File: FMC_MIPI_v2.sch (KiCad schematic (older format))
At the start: 1 part

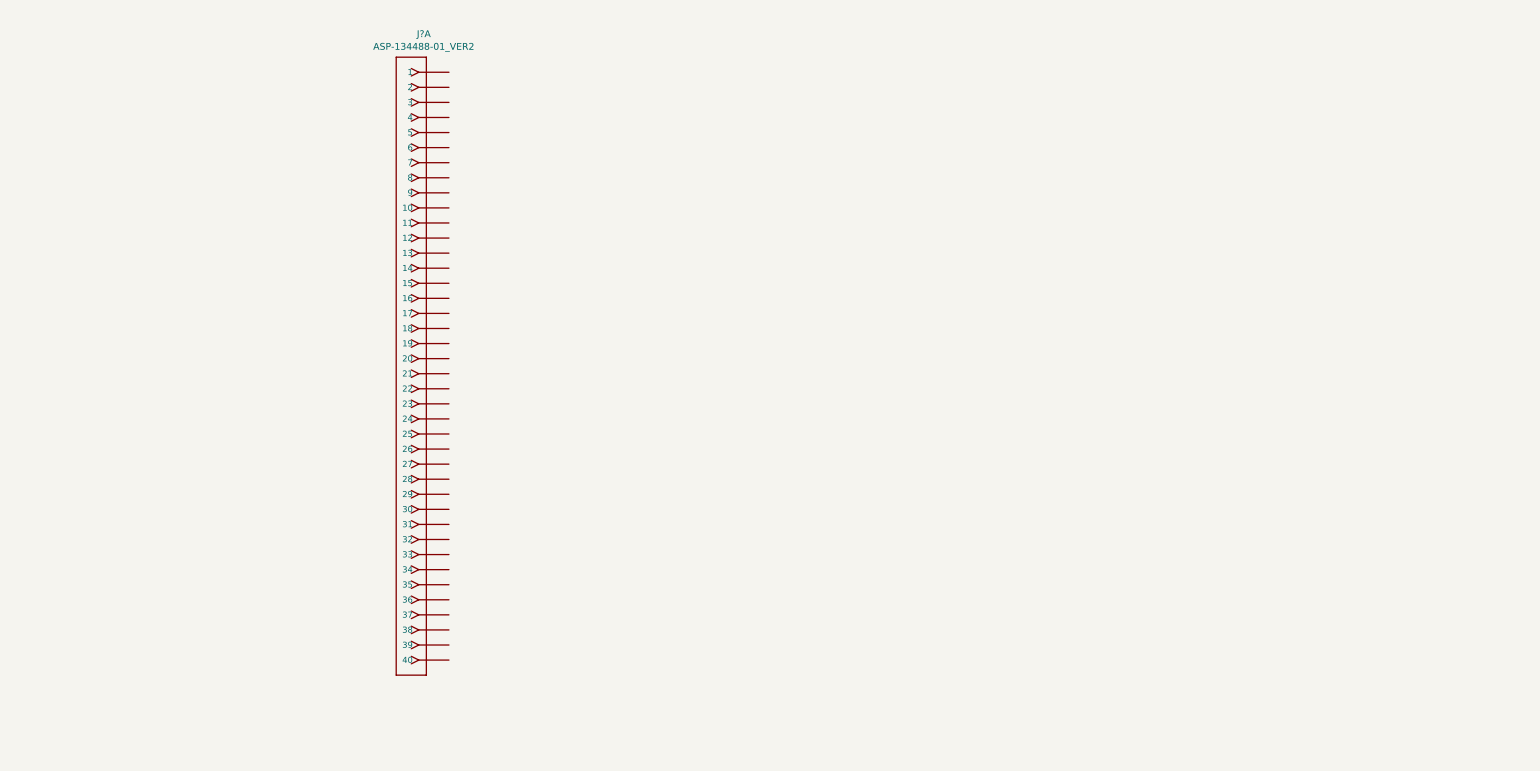
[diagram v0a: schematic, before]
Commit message: adding lvds to slvs
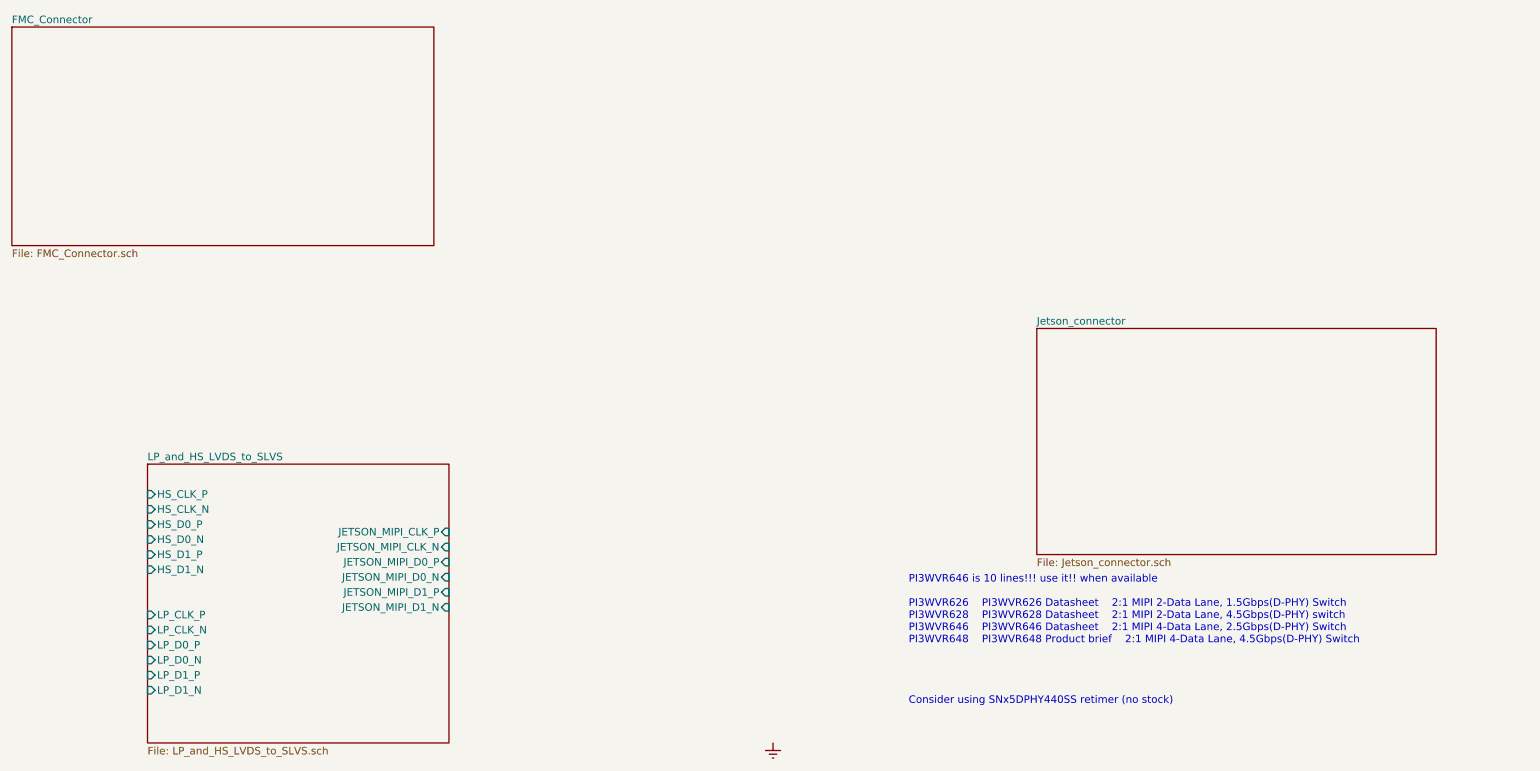
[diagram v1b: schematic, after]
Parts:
- removed J?: ASP-134488-01_VER2, symbol FMC_MIPI_v2:ASP-134488-01_VER2
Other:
- note added: "PI3WVR646 is 10 lines!!! use it!! when available\n\nPI3WVR626 PI3WVR626 Datasheet 2:1 MIPI 2-Data Lane, 1.5Gbps(D-PHY) Switch\nPI3WVR628 PI3WVR628 Datasheet 2:1 MIPI 2-Data Lane, 4.5Gbps(D-PHY) switch\nPI3WVR646 PI3WVR646 Datasheet 2:1 MIPI 4-Data Lane, 2.5Gbps(D-PHY) Switch\nPI3WVR648 PI3WVR648 Product brief 2:1 MIPI 4-Data Lane, 4.5Gbps(D-PHY) Switch\n \n\n\n\nConsider using SNx5DPHY440SS retim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"
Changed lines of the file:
@@
 $Descr A4 11693 8268
 encoding utf-8
-Sheet 1 1
+Sheet 1 10
 Title ""
 Date ""
@@
 Comment4 ""
 $EndDescr
+$Sheet
+S 900  850  2800 1450
+U 6170B975
+F0 "FMC_Connector" 50
+F1 "FMC_Connector.sch" 50
+$EndSheet
+$Sheet
+S 7700 2850 2650 1500
+U 61ACA102
+F0 "Jetson_connector" 50
+F1 "Jetson_connector.sch" 50
+$EndSheet
 $Comp
-L FMC_MIPI_v2:ASP-134488-01_VER2 J?
-U 1 1 61431E0F
-P 3400 3400
-F 0 "J?" H 3633 5904 45  0000 C CNN
-F 1 "ASP-134488-01_VER2" H 3633 5820 45  0000 C CNN
-F 2 "" H 3400 3700 60  0001 C CNN
-F 3 "" H 3400 3700 60  0001 C CNN
-	1    3400 3400
+L FMC_MIPI_v2:Earth #PWR0101
+U 1 1 61B01356
+P 5950 5600
+F 0 "#PWR0101" H 5950 5350 50  0001 C CNN
+F 1 "Earth" H 5950 5450 50  0001 C CNN
+F 2 "" H 5950 5600 50  0001 C CNN
+F 3 "~" H 5950 5600 50  0001 C CNN
+	1    5950 5600
 	1    0    0    -1
 $EndComp
+Text Notes 6850 5350 0    50   ~ 0
+PI3WVR646 is 10 lines!!! use it!! when available\n\nPI3WVR626	PI3WVR626 Datasheet	2:1 MIPI 2-Data Lane, 1.5Gbps(D-PHY) Switch\nPI3WVR628	PI3WVR628 Datasheet	2:1 MIPI 2-Data Lane, 4.5Gbps(D-PHY) switch\nPI3WVR646	PI3WVR646 Datasheet	2:1 MIPI 4-Data Lane, 2.5Gbps(D-PHY) Switch\nPI3WVR648	PI3WVR648 Product brief	2:1 MIPI 4-Data Lane, 4.5Gbps(D-PHY) Switch\n		\n\n\n\nConsider using SNx5DPHY440SS retimer (no stock)
+$Sheet
+S 1800 3750 2000 1850
+U 6193F705
+F0 "LP_and_HS_LVDS_to_SLVS" 50
+F1 "LP_and_HS_LVDS_to_SLVS.sch" 50
+F2 "JETSON_MIPI_CLK_P" I R 3800 4200 50
+F3 "JETSON_MIPI_CLK_N" I R 3800 4300 50
+F4 "JETSON_MIPI_D0_P" I R 3800 4400 50
+F5 "JETSON_MIPI_D1_P" I R 3800 4600 50
+F6 "JETSON_MIPI_D1_N" I R 3800 4700 50
+F7 "JETSON_MIPI_D0_N" I R 3800 4500 50
+F8 "HS_CLK_P" I L 1800 3950 50
+F9 "HS_CLK_N" I L 1800 4050 50
+F10 "HS_D0_P" I L 1800 4150 50
+F11 "HS_D1_P" I L 1800 4350 50
+F12 "HS_D1_N" I L 1800 4450 50
+F13 "HS_D0_N" I L 1800 4250 50
+F14 "LP_CLK_P" I L 1800 4750 50
+F15 "LP_CLK_N" I L 1800 4850 50
+F16 "LP_D0_P" I L 1800 4950 50
+F17 "LP_D1_P" I L 1800 5150 50
+F18 "LP_D1_N" I L 1800 5250 50
+F19 "LP_D0_N" I L 1800 5050 50
+$EndSheet
 $EndSCHEMATC

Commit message: just commit
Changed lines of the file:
@@
 $Descr A4 11693 8268
 encoding utf-8
-Sheet 1 10
+Sheet 1 46
 Title ""
 Date ""
@@
 PI3WVR646 is 10 lines!!! use it!! when available\n\nPI3WVR626	PI3WVR626 Datasheet	2:1 MIPI 2-Data Lane, 1.5Gbps(D-PHY) Switch\nPI3WVR628	PI3WVR628 Datasheet	2:1 MIPI 2-Data Lane, 4.5Gbps(D-PHY) switch\nPI3WVR646	PI3WVR646 Datasheet	2:1 MIPI 4-Data Lane, 2.5Gbps(D-PHY) Switch\nPI3WVR648	PI3WVR648 Product brief	2:1 MIPI 4-Data Lane, 4.5Gbps(D-PHY) Switch\n		\n\n\n\nConsider using SNx5DPHY440SS retimer (no stock)
 $Sheet
-S 1800 3750 2000 1850
-U 6193F705
-F0 "LP_and_HS_LVDS_to_SLVS" 50
-F1 "LP_and_HS_LVDS_to_SLVS.sch" 50
-F2 "JETSON_MIPI_CLK_P" I R 3800 4200 50
-F3 "JETSON_MIPI_CLK_N" I R 3800 4300 50
-F4 "JETSON_MIPI_D0_P" I R 3800 4400 50
-F5 "JETSON_MIPI_D1_P" I R 3800 4600 50
-F6 "JETSON_MIPI_D1_N" I R 3800 4700 50
-F7 "JETSON_MIPI_D0_N" I R 3800 4500 50
-F8 "HS_CLK_P" I L 1800 3950 50
-F9 "HS_CLK_N" I L 1800 4050 50
-F10 "HS_D0_P" I L 1800 4150 50
-F11 "HS_D1_P" I L 1800 4350 50
-F12 "HS_D1_N" I L 1800 4450 50
-F13 "HS_D0_N" I L 1800 4250 50
-F14 "LP_CLK_P" I L 1800 4750 50
-F15 "LP_CLK_N" I L 1800 4850 50
-F16 "LP_D0_P" I L 1800 4950 50
-F17 "LP_D1_P" I L 1800 5150 50
-F18 "LP_D1_N" I L 1800 5250 50
-F19 "LP_D0_N" I L 1800 5050 50
+S 2450 2950 1000 1050
+U 6191D89C
+F0 "LVDS_to_Jetson_lines" 50
+F1 "LVDS_to_Jetson_lines.sch" 50
+F2 "SWITCH_VDD_VADJ" I L 2450 3100 50
+F3 "SWITCH_SEL_CAM_A" I L 2450 3400 50
+F4 "SWITCH_SEL_CAM_B" I L 2450 3500 50
+F5 "SWITCH_SEL_CAM_C" I L 2450 3600 50
+F6 "SWITCH_SEL_CAM_D" I L 2450 3700 50
+F7 "SWITCH_SEL_CAM_E" I L 2450 3800 50
+F8 "SWITCH_SEL_CAM_F" I L 2450 3900 50
 $EndSheet
 $EndSCHEMATC
